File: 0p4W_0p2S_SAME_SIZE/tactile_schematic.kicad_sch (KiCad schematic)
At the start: 55 parts, among them IC1 CY8C4145PVI-PS431, J1 Conn_01x03, J2 Conn_01x04, J3 Conn_01x04, J4 Conn_01x03, J5 Conn_ARM_SWD_TagConnect_TC203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

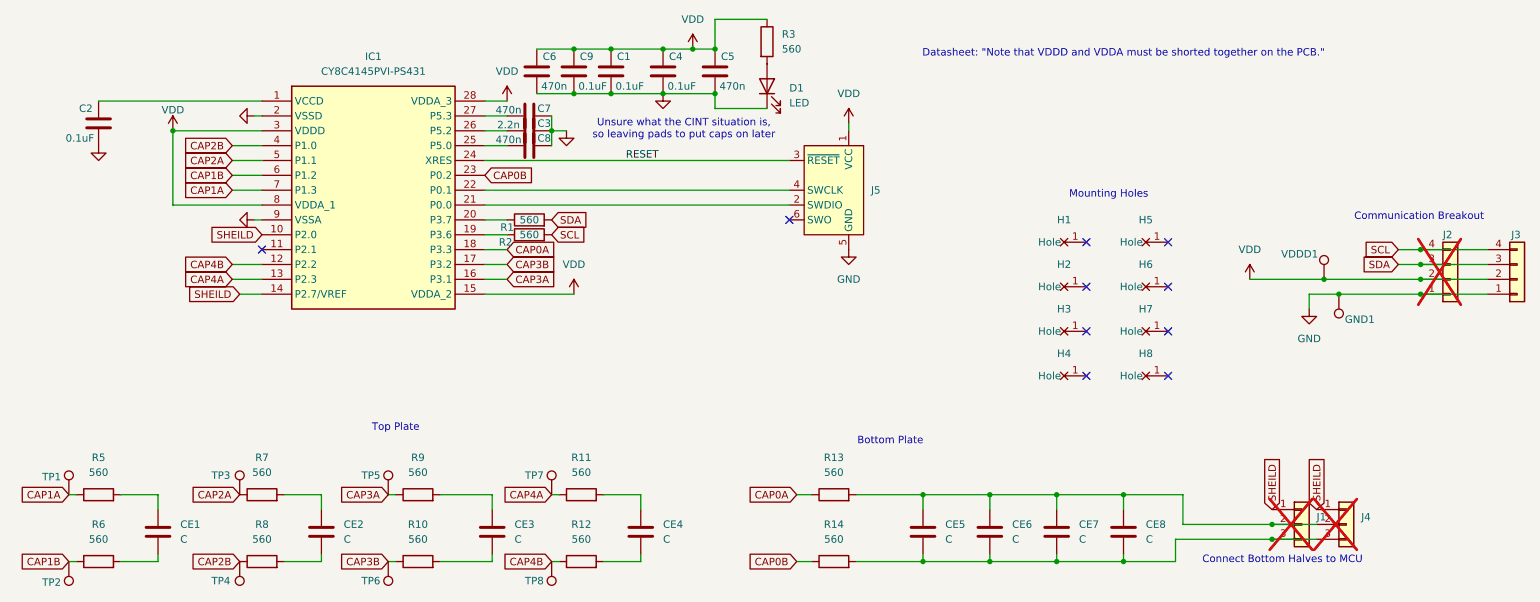
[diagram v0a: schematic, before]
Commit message: fixed silkscreen
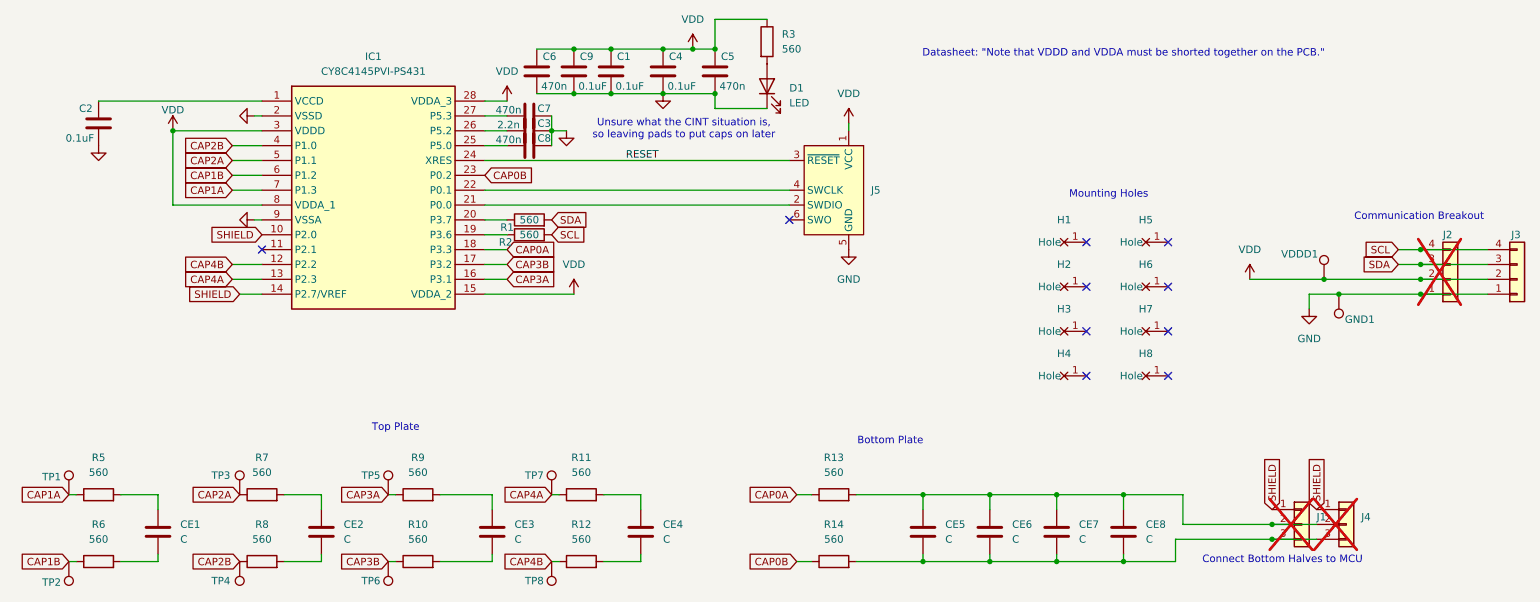
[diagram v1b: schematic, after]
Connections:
- net SHEILD renamed SHIELD
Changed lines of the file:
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@@
 		)
 	)
-	(global_label "SHEILD"
+	(global_label "SHIELD"
 		(shape input)
 		(at 228.6 99.06 90)
@@
 		)
 	)
-	(global_label "SHEILD"
+	(global_label "SHIELD"
 		(shape input)
 		(at 55.88 52.07 180)
@@
 		)
 	)
-	(global_label "SHEILD"
+	(global_label "SHIELD"
 		(shape input)
 		(at 52.07 62.23 180)
@@
 		)
 	)
-	(global_label "SHEILD"
+	(global_label "SHIELD"
 		(shape input)
 		(at 236.22 99.06 90)
